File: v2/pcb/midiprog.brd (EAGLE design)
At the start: 99.1 x 78.7 mm, 56 parts, among them IC1 PIC18F4550_40, IC2 TPIC6B596N, IC4 TPIC6B596N, Q2 2N2222A, Q3 2N2222A, Q4 2N2222A, Q5 8MHz

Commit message: Named connections better on schematic.
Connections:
- net N$46 renamed BTN_TOP_6
- net N$47 renamed BTN_BOT_6
- net N$48 renamed BTN_TOP_8
- net N$49 renamed BTN_TOP_7
- net N$50 renamed BTN_BOT_8
- net N$51 renamed BTN_BOT_7
- net N$52 renamed BTN_BOT_5
- net N$55 renamed BTN_BOT_4
- net N$56 renamed BTN_BOT_1
- net N$57 renamed BTN_BOT_2
- net N$58 renamed BTN_BOT_3
- net N$60 renamed BTN_TOP_5
- net N$61 renamed BTN_TOP_4
- net N$62 renamed BTN_TOP_1
- net N$63 renamed BTN_TOP_2
- net N$64 renamed BTN_TOP_3
- net SHIFTREG_SCL renamed SHIFTREG_SCK
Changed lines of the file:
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@@
 <wire x1="53.34" y1="54.61" x2="59.69" y2="54.61" width="0.254" layer="16"/>
 </signal>
-<signal name="SHIFTREG_SCL">
+<signal name="SHIFTREG_SCK">
 <contactref element="IC2" pad="13"/>
 <contactref element="IC1" pad="3"/>
@@
 <wire x1="39.37" y1="59.69" x2="39.37" y2="57.15" width="0.4064" layer="1"/>
 </signal>
-<signal name="N$46">
+<signal name="BTN_TOP_6">
 <contactref element="U$2" pad="5"/>
 <contactref element="BTN_FX_CN" pad="9"/>
@@
 <wire x1="13.97" y1="8.89" x2="16.51" y2="6.35" width="0.254" layer="1"/>
 </signal>
-<signal name="N$48">
+<signal name="BTN_TOP_8">
 <contactref element="U$2" pad="4"/>
 <contactref element="BTN_FX_CN" pad="11"/>
@@
 <wire x1="10.16" y1="10.16" x2="13.97" y2="6.35" width="0.254" layer="1"/>
 </signal>
-<signal name="N$49">
+<signal name="BTN_TOP_7">
 <contactref element="BTN_FX_CN" pad="13"/>
 <contactref element="U$2" pad="2"/>
@@
 <wire x1="8.89" y1="8.89" x2="11.43" y2="6.35" width="0.254" layer="1"/>
 </signal>
-<signal name="N$60">
+<signal name="BTN_TOP_5">
 <contactref element="BTN_FX_CN" pad="15"/>
 <contactref element="U$2" pad="1"/>
@@
 <wire x1="7.62" y1="7.62" x2="8.89" y2="6.35" width="0.254" layer="1"/>
 </signal>
-<signal name="N$61">
+<signal name="BTN_TOP_4">
 <contactref element="BTN_FX_CN" pad="7"/>
 <contactref element="U$2" pad="12"/>
@@
 <wire x1="17.78" y1="7.62" x2="19.05" y2="6.35" width="0.254" layer="1"/>
 </signal>
-<signal name="N$62">
+<signal name="BTN_TOP_1">
 <contactref element="BTN_FX_CN" pad="5"/>
 <contactref element="U$2" pad="13"/>
@@
 <wire x1="21.59" y1="20.32" x2="21.59" y2="6.35" width="0.254" layer="1"/>
 </signal>
-<signal name="N$63">
+<signal name="BTN_TOP_2">
 <contactref element="BTN_FX_CN" pad="3"/>
 <contactref element="U$2" pad="14"/>
@@
 <wire x1="22.86" y1="7.62" x2="24.13" y2="6.35" width="0.254" layer="1"/>
 </signal>
-<signal name="N$64">
+<signal name="BTN_TOP_3">
 <contactref element="BTN_FX_CN" pad="1"/>
 <contactref element="U$2" pad="15"/>
@@
 <wire x1="24.13" y1="8.89" x2="26.67" y2="6.35" width="0.254" layer="1"/>
 </signal>
-<signal name="N$47">
+<signal name="BTN_BOT_6">
 <contactref element="BTN_PR_CN" pad="9"/>
 <contactref element="U$1" pad="5"/>
@@
 <wire x1="38.1" y1="8.89" x2="40.64" y2="6.35" width="0.254" layer="1"/>
 </signal>
-<signal name="N$50">
+<signal name="BTN_BOT_8">
 <contactref element="BTN_PR_CN" pad="11"/>
 <contactref element="U$1" pad="4"/>
@@
 <wire x1="34.29" y1="10.16" x2="38.1" y2="6.35" width="0.254" layer="1"/>
 </signal>
-<signal name="N$51">
+<signal name="BTN_BOT_7">
 <contactref element="BTN_PR_CN" pad="13"/>
 <contactref element="U$1" pad="2"/>
@@
 <wire x1="33.02" y1="8.89" x2="35.56" y2="6.35" width="0.254" layer="1"/>
 </signal>
-<signal name="N$52">
+<signal name="BTN_BOT_5">
 <contactref element="BTN_PR_CN" pad="15"/>
 <contactref element="U$1" pad="1"/>
@@
 <wire x1="31.75" y1="7.62" x2="33.02" y2="6.35" width="0.254" layer="1"/>
 </signal>
-<signal name="N$55">
+<signal name="BTN_BOT_4">
 <contactref element="BTN_PR_CN" pad="7"/>
 <contactref element="U$1" pad="12"/>
@@
 <wire x1="41.91" y1="7.62" x2="43.18" y2="6.35" width="0.254" layer="1"/>
 </signal>
-<signal name="N$56">
+<signal name="BTN_BOT_1">
 <contactref element="BTN_PR_CN" pad="5"/>
 <contactref element="U$1" pad="13"/>
@@
 <wire x1="45.72" y1="20.32" x2="45.72" y2="6.35" width="0.254" layer="1"/>
 </signal>
-<signal name="N$57">
+<signal name="BTN_BOT_2">
 <contactref element="BTN_PR_CN" pad="3"/>
 <contactref element="U$1" pad="14"/>
@@
 <wire x1="46.99" y1="7.62" x2="48.26" y2="6.35" width="0.254" layer="1"/>
 </signal>
-<signal name="N$58">
+<signal name="BTN_BOT_3">
 <contactref element="BTN_PR_CN" pad="1"/>
 <contactref element="U$1" pad="15"/>

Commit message: Renamed pins and connectors on schematic and added proper labels.
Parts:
- renumbered BTN_FX_CN to BTN_TOP_CN, BTN_PR_CN to BTN_BOT_CN, LED_FX_CN to LED_TOP_CN, LED_PR_CN to LED_BOT_CN
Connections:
- net N$10 renamed LED_TOP_3
- net N$11 renamed LED_TOP_4
- net N$12 renamed LED_TOP_5
- net N$13 renamed LED_TOP_6
- net N$14 renamed LED_TOP_7
- net N$15 renamed LED_TOP_8
- net N$2 renamed LED_TOP_1
- net N$24 renamed LED_BOT_2
- net N$27 renamed LED_BOT_3
- net N$28 renamed LED_BOT_4
- net N$3 renamed LED_TOP_2
- net N$30 renamed LED_BOT_5
- net N$32 renamed LED_BOT_6
- net N$36 renamed LED_BOT_7
- net N$37 renamed LED_BOT_8
- net N$6 renamed LED_BOT_1

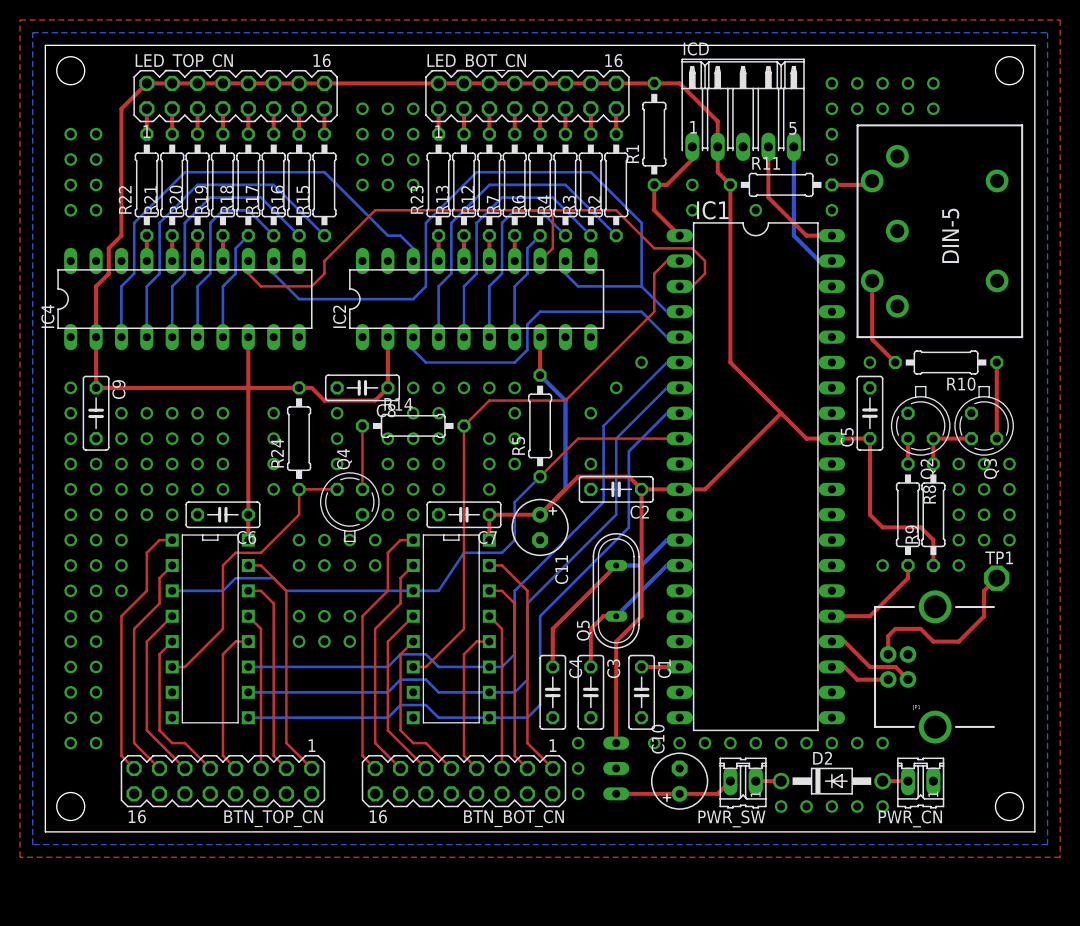
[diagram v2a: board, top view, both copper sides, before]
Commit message: Rotated board 180 deg and removed extra vias.
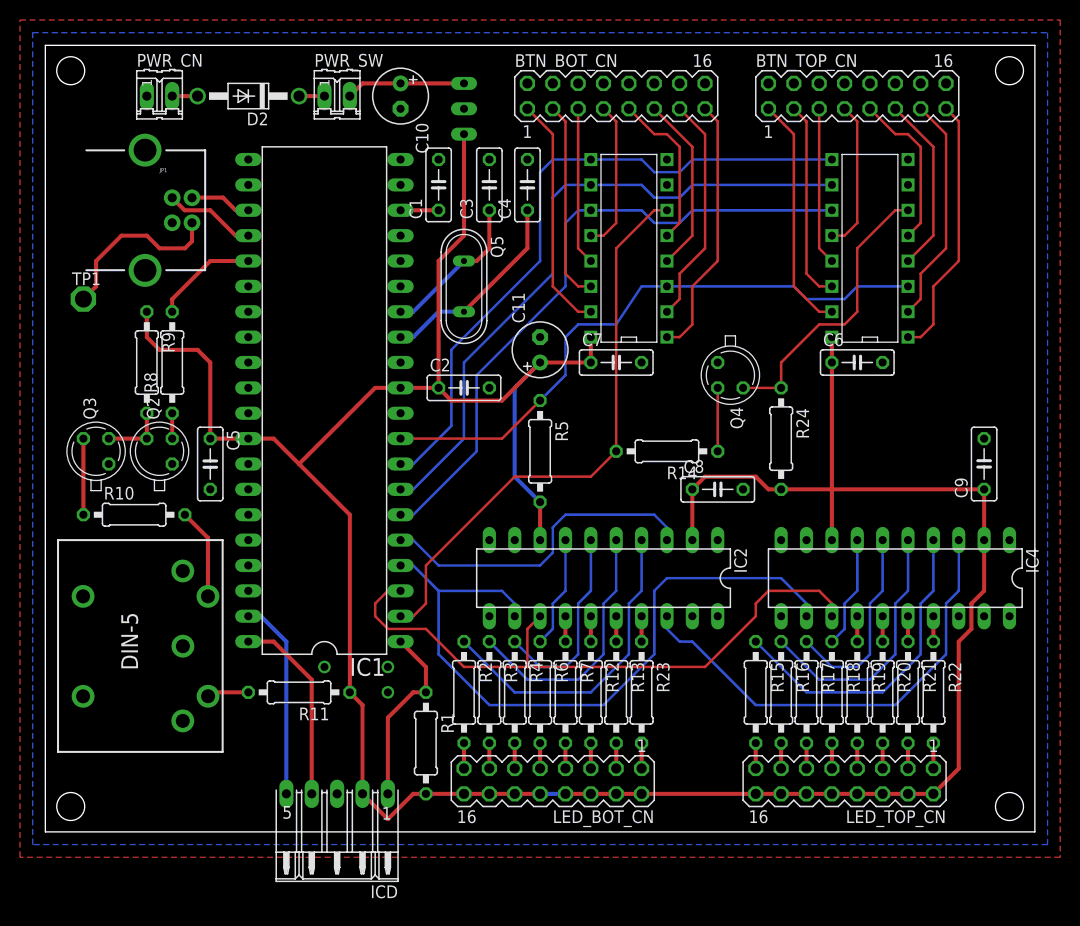
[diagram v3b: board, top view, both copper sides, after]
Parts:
- moved PWR_CN 102.5 mm to (11.4, 73.7), turned to 0 degrees
- moved TP1 95.6 mm to (3.81, 53.3)
- moved R22 93.7 mm to (88.9, 14.0), turned to 270 degrees
- moved BTN_TOP_CN 93.5 mm to (81.3, 73.7), turned to 0 degrees
- moved LED_TOP_CN 91.8 mm to (80.0, 5.08), turned to 180 degrees
- moved D2 90.1 mm to (20.3, 73.7), turned to 180 degrees
- moved R21 89.5 mm to (86.4, 14.0), turned to 270 degrees
- moved C9 89.0 mm to (94.0, 36.8), turned to 90 degrees
- moved Q3 88.9 mm to (5.08, 38.1), turned to 90 degrees
- moved MIDI_OUT 88.6 mm to (10.2, 19.1), turned to 270 degrees
- moved JP1 86.7 mm to (12.7, 62.2), turned to 0 degrees
- moved R20 85.3 mm to (83.8, 14.0), turned to 270 degrees
- moved R10 82.7 mm to (8.89, 31.8), turned to 0 degrees
- moved R19 81.3 mm to (81.3, 14.0), turned to 270 degrees
- moved R9 80.2 mm to (10.2, 47.0), turned to 270 degrees
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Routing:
- net N$1: track 12.3 -> 18.6 mm
- net N$16: track 13.8 -> 20.1 mm
- net N$17: track 13.0 -> 19.4 mm
- net VDD: track 289.7 -> 294.0 mm
